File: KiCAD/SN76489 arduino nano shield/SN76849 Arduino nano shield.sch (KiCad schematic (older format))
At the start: 10 parts, among them J1 Arduino_sn, P1 Audio_uit, P3 I2C, U1 PCF8574, U2 LM358, U3 SN76489

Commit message: Printplaat 20180601 0.5 laat maak
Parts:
- added J2: audio_debug, Socket_Strips:Socket_Strip_Straight_1x02_Pitch2.54mm, symbol Conn_01x02
- C2, C3: footprint Capacitors_SMD:C_1210 -> Capacitors_THT:CP_Radial_D8.0mm_P2.50mm
- R2: footprint Resistors_SMD:R_1206 -> w_pth_resistors:RC03
- RV1: footprint w_pth_resistors:trimmer_alps-rk09k1130ah1 -> w_pth_resistors:trimmer_ecp_ca9-v10
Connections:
- net GND: now also J2.2 (Pin_2)
- net at C2.2, R2.2: now also J2.1 (Pin_1)
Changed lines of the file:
@@
 Sheet 1 1
 Title "SN76489 geluid shield vir Arduino Nano"
-Date "2018-04-05"
-Rev "0.3 20180405"
+Date "2018-05-16"
+Rev "20180601 0.5"
 Comp "EasyLab4Kids"
 Comment1 "Ontwerp: Michiel Erasmus"
@@
 F 0 "C3" H 7110 4460 38  0000 L CNN
 F 1 "CP_220uF" V 6990 4240 30  0000 L CNN
-F 2 "Capacitors_SMD:C_1210" H 7100 4390 50  0001 C CNN
+F 2 "Capacitors_THT:CP_Radial_D8.0mm_P2.50mm" H 7100 4390 50  0001 C CNN
 F 3 "" H 7100 4390 50  0001 C CNN
 	1    7100 4390
@@
 F 0 "RV1" H 7490 4310 38  0000 C CNN
 F 1 "POT_50k" H 7490 4390 30  0000 C CNN
-F 2 "w_pth_resistors:trimmer_alps-rk09k1130ah1" H 7490 4390 50  0001 C CNN
+F 2 "w_pth_resistors:trimmer_ecp_ca9-v10" H 7490 4390 50  0001 C CNN
 F 3 "" H 7490 4390 50  0000 C CNN
 	1    7490 4390
@@
 F 0 "R2" H 6090 4620 38  0000 L CNN
 F 1 "R1k" V 6060 4560 30  0000 L CNN
-F 2 "Resistors_SMD:R_1206" H 6060 4600 50  0001 C CNN
+F 2 "w_pth_resistors:RC03" H 6060 4600 50  0001 C CNN
 F 3 "" H 6060 4600 50  0000 C CNN
 	1    6060 4600
@@
 F 0 "C2" H 6070 4990 38  0000 L CNN
 F 1 "CP_10uF" V 5950 4770 30  0000 L CNN
-F 2 "Capacitors_SMD:C_1210" H 6060 4920 50  0001 C CNN
+F 2 "Capacitors_THT:CP_Radial_D8.0mm_P2.50mm" H 6060 4920 50  0001 C CNN
 F 3 "" H 6060 4920 50  0001 C CNN
 	1    6060 4920
@@
 	1    0    0    -1
 $EndComp
+$Comp
+L Conn_01x02 J2
+U 1 1 5AEF7BF4
+P 5140 4730
+F 0 "J2" H 5140 4830 50  0000 C CNN
+F 1 "audio_debug" H 5140 4530 30  0000 C CNN
+F 2 "Socket_Strips:Socket_Strip_Straight_1x02_Pitch2.54mm" H 5140 4730 50  0001 C CNN
+F 3 "" H 5140 4730 50  0001 C CNN
+	1    5140 4730
+	-1   0    0    1
+$EndComp
 Wire Wire Line
 	5600 1110 6050 1110
@@
 	5650 1610 5650 1810
 Connection ~ 5650 1810
+Wire Wire Line
+	5340 4730 6060 4730
+Connection ~ 6060 4730
+Wire Wire Line
+	5340 4630 5950 4630
+Connection ~ 5950 4630
 $EndSCHEMATC

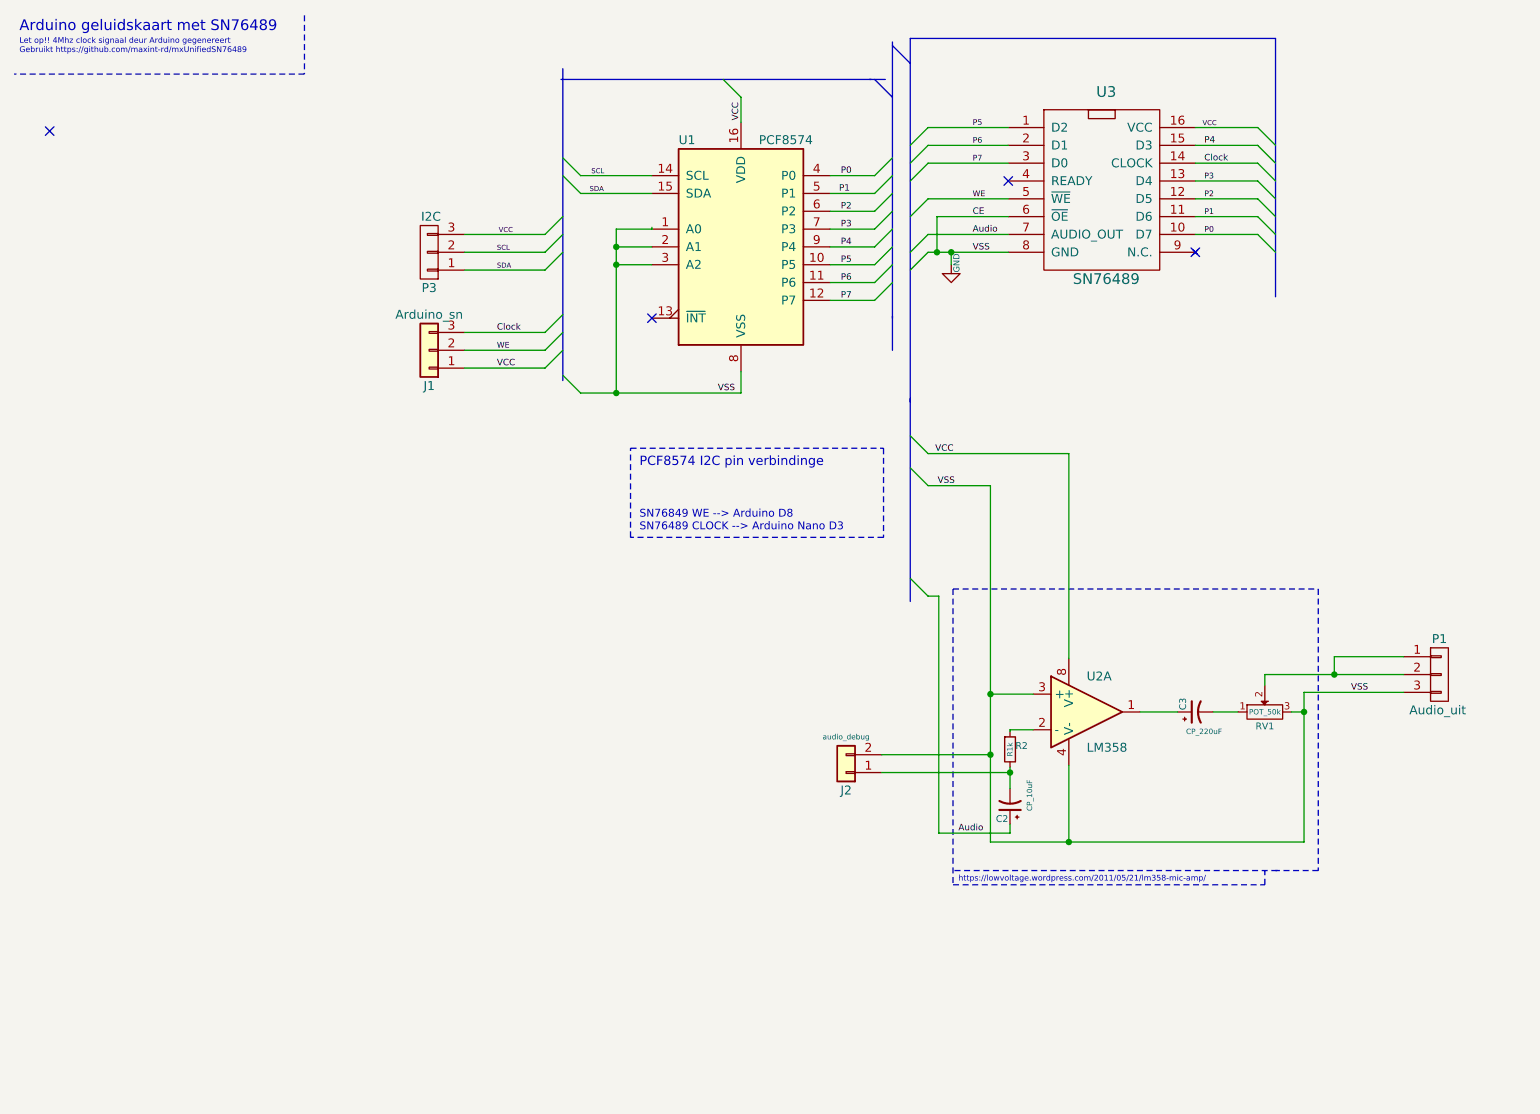
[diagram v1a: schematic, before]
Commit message: toevoeging OpAmp schema en PCB 20180617 0.7
daar is nog een bug. Op printplaat capacitor C1 posetief niet
verobonden!
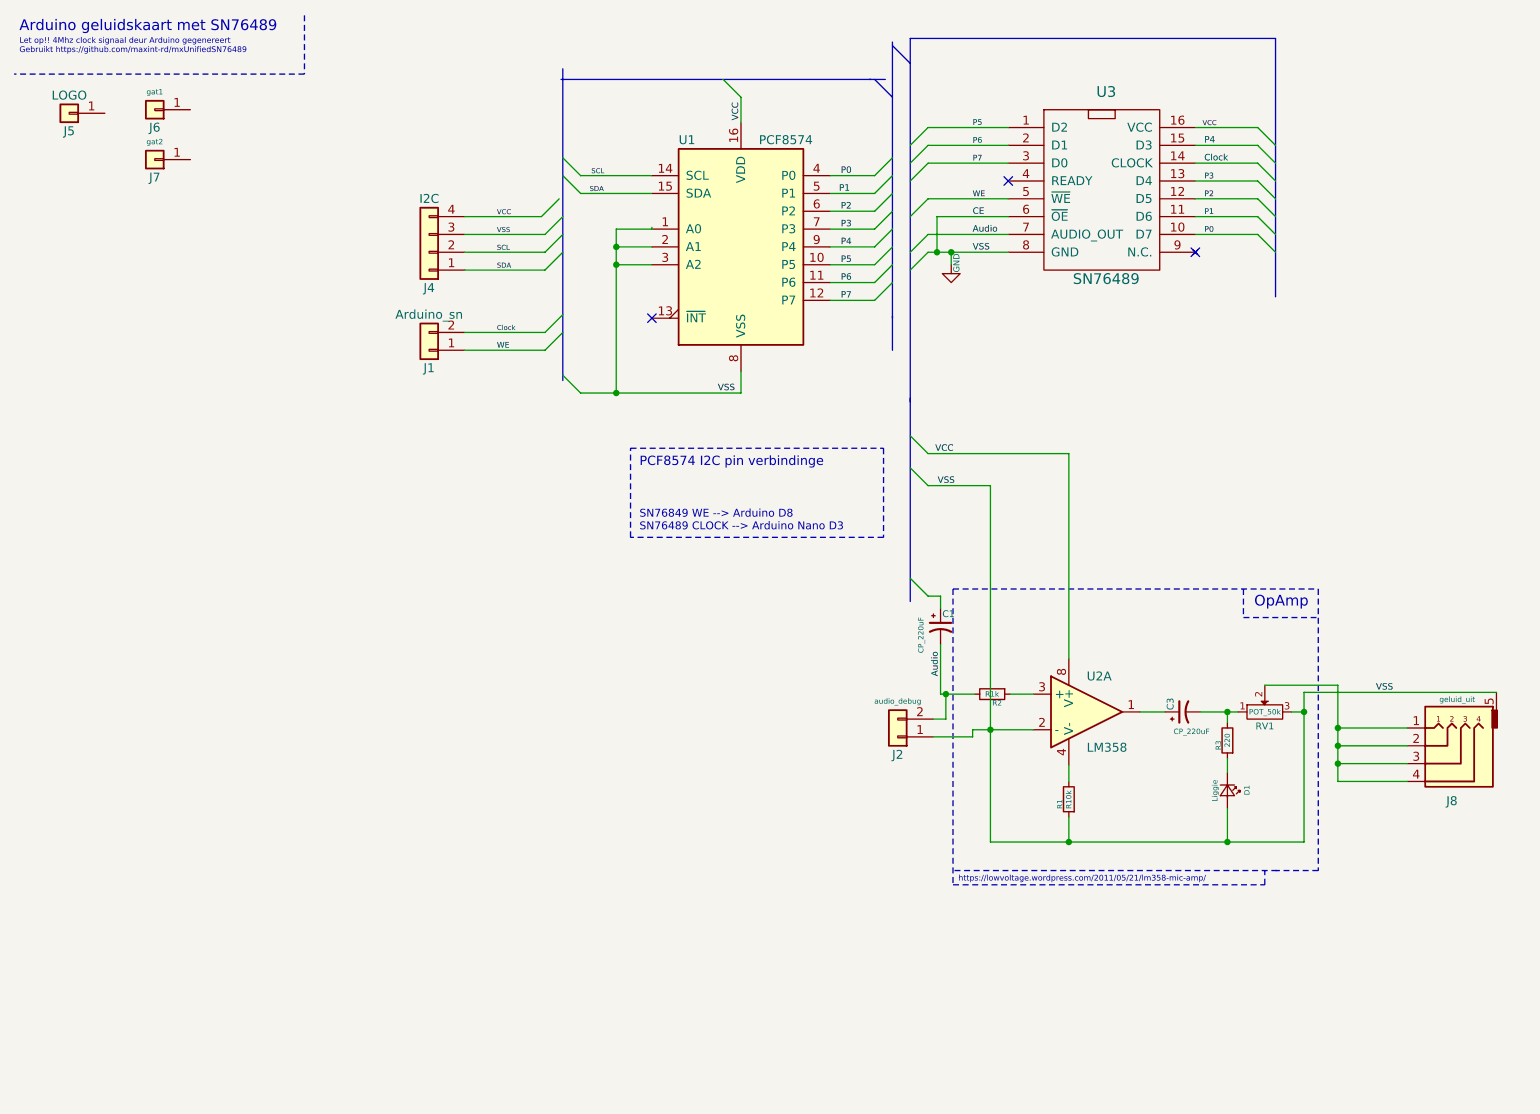
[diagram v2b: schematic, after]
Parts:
- removed C2: CP_10uF, Capacitors_THT:CP_Radial_D8.0mm_P2.50mm, symbol CP1_Small
- removed J1: Arduino_sn, Socket_Strips:Socket_Strip_Angled_1x03_Pitch2.54mm, symbol Conn_01x03
- removed P1: Audio_uit, Socket_Strips:Socket_Strip_Angled_1x03_Pitch2.54mm, symbol CONN_01X03
- removed P3: I2C, Socket_Strips:Socket_Strip_Angled_1x03_Pitch2.54mm, symbol CONN_01X03
- added C1: CP_220uF, Capacitors_THT:CP_Radial_D8.0mm_P2.50mm, symbol CP1_Small
- added D1: Liggie, LEDs:LED_D3.0mm, symbol LED_Small
- added J1: Arduino_sn, Pin_Headers:Pin_Header_Angled_1x02_Pitch2.54mm, symbol Conn_01x02
- added J4: I2C, Pin_Headers:Pin_Header_Angled_1x04_Pitch2.54mm, symbol Conn_01x04
- added J5: LOGO, lib_michiel:Sovjet_simpits_logo01, symbol Conn_01x01
- added J6: gat1, Mounting_Holes:MountingHole_2.5mm_Pad, symbol Conn_01x01
- added J7: gat2, Mounting_Holes:MountingHole_2.5mm_Pad, symbol Conn_01x01
- added J8: geluid_uit, lib_michiel:3.5mm_stereo_TRS_jack_A-853_Tayda_, symbol Audio-Jack-5
- added R1: R10k, w_pth_resistors:RC03, symbol R_Small
- added R3: 220, w_pth_resistors:RC03, symbol R_Small
- J2: footprint Socket_Strips:Socket_Strip_Straight_1x02_Pitch2.54mm -> Pin_Headers:Pin_Header_Angled_1x02_Pitch2.54mm
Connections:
- net Audio: now also J2.2 (Pin_2), R2.2, C1.2
- net Clock: now also J1.2 (Pin_2)
- net GND: now also J2.1 (Pin_1), U2.2 (-), D1.2 (A), J4.3 (Pin_3), J8.5, R1.1; no longer J2.2 (Pin_2), U2.3 (+), U2.4 (V-)
- net SCL: now also J4.2 (Pin_2)
- net SDA: now also J4.1 (Pin_1)
- net VCC: now also J4.4 (Pin_4)
- net WE: now also J1.1 (Pin_1)
- net at RV1.2: now also J8.1, J8.2, J8.3, J8.4
- net at C3.2, RV1.1: now also R3.2
- net at R2.1: now also U2.3 (+); no longer U2.2 (-)
- new net: R1.2, U2.4 (V-)
- new net: D1.1 (K), R3.1
- no-connect marks 4 -> 3
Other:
- note added: "OpAmp"
- moved on the sheet: C3, J2, R2

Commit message: DERC fails opgelost 20180617 0.7.01
'n paar nets ontbreekte conneksies op de printplaat.
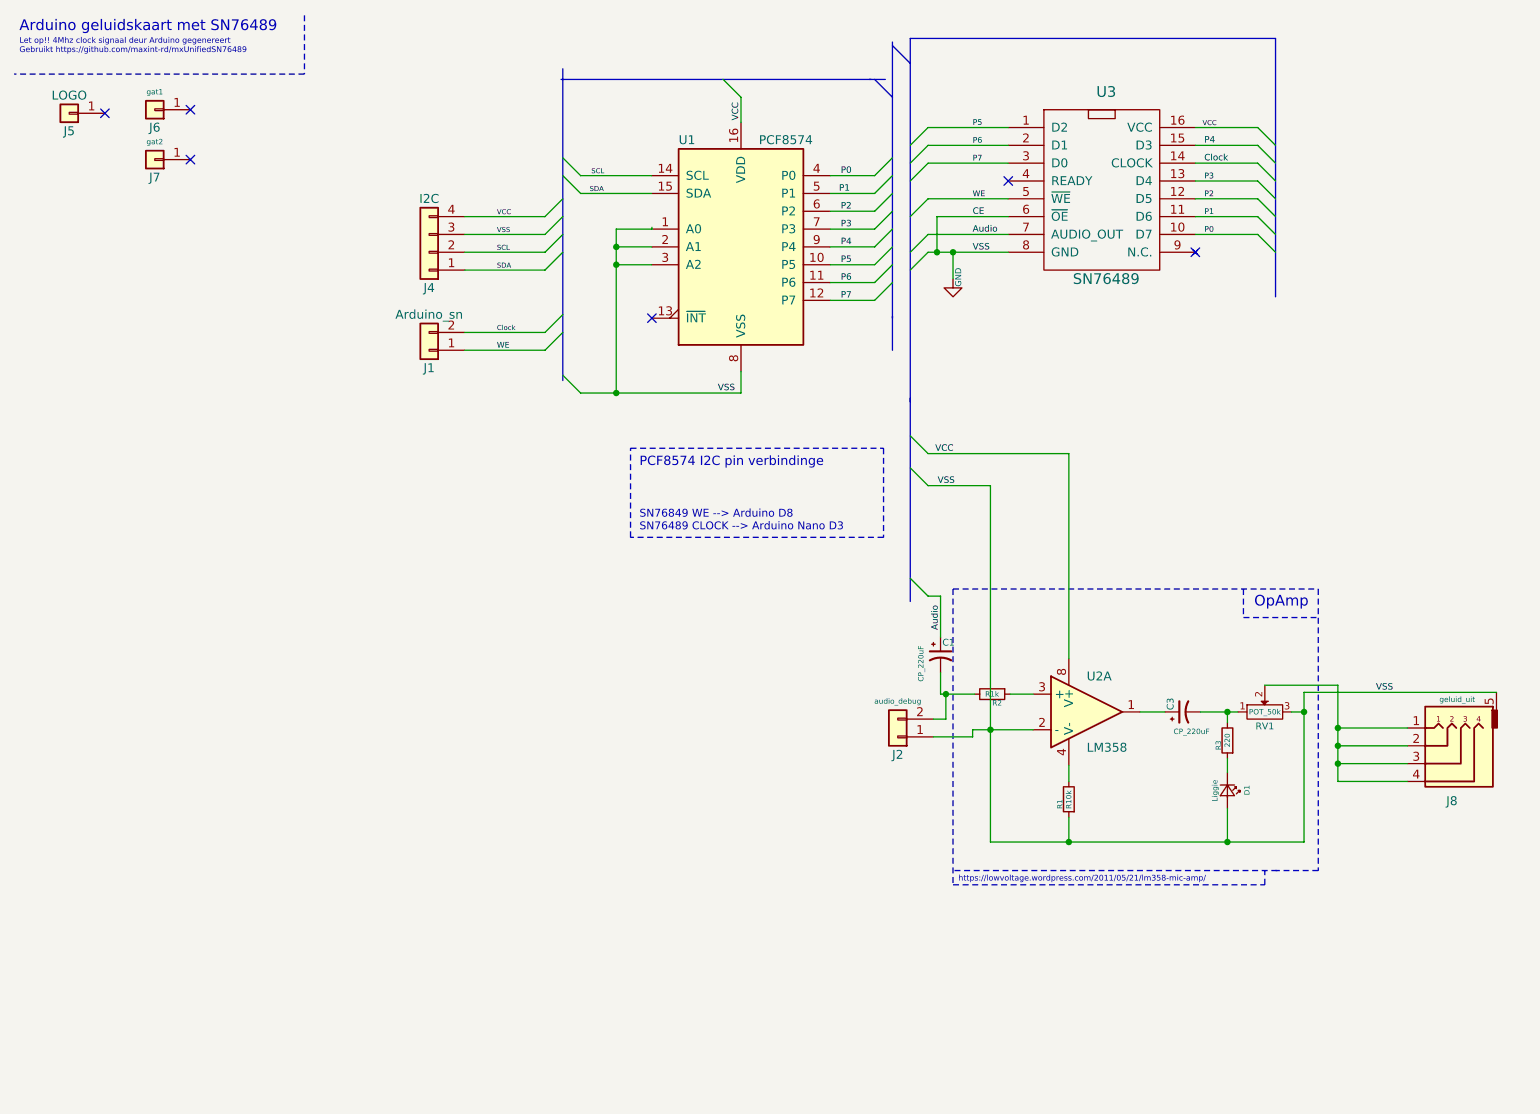
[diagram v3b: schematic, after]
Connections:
- net Audio: now also C1.1; no longer C1.2, J2.2 (Pin_2), R2.2
- new net: C1.2, J2.2 (Pin_2), R2.2
- no-connect marks 3 -> 6
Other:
- moved on the sheet: C1
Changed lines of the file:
@@
 Sheet 1 1
 Title "SN76489 geluid shield vir Arduino Nano"
-Date "2018-06-17"
-Rev "20180617 0.7"
+Date "2018-06-24"
+Rev "20180617 0.7.01"
 Comp "EasyLab4Kids"
 Comment1 "Ontwerp: Michiel Erasmus"
@@
 Text Label 5750 3120 2    36   ~ 0
 VSS
-Entry Wire Line
-	5500 3020 5600 3120
 Text Label 5640 2940 0    36   ~ 0
 VCC
@@
 Text Notes 5770 5350 0    32   ~ 0
 https://lowvoltage.wordpress.com/2011/05/21/lm358-mic-amp/
-Entry Wire Line
-	5500 3640 5600 3740
-Text Label 5670 4190 1    36   ~ 0
+Text Label 5670 3930 1    36   ~ 0
 Audio
 $Comp
 L GND #PWR01
 U 1 1 5A9BDD7A
-P 5730 1880
-F 0 "#PWR01" H 5730 1630 50  0001 C CNN
-F 1 "GND" V 5760 1890 34  0000 C CNN
-F 2 "" H 5730 1880 50  0000 C CNN
-F 3 "" H 5730 1880 50  0000 C CNN
-	1    5730 1880
+P 5740 1960
+F 0 "#PWR01" H 5740 1710 28  0001 C CNN
+F 1 "GND" V 5770 1970 34  0000 C CNN
+F 2 "" H 5740 1960 50  0000 C CNN
+F 3 "" H 5740 1960 50  0000 C CNN
+	1    5740 1960
 	1    0    0    -1
 $EndComp
@@
 $EndComp
 Entry Wire Line
-	3430 1610 3530 1510
+	3450 1610 3550 1510
 Text Label 3180 1710 0    28   ~ 0
 VSS
@@
 	-1   0    0    1
 $EndComp
+$Comp
+L CP1_Small C1
+U 1 1 5B26BD41
+P 5670 4070
+F 0 "C1" H 5680 4140 38  0000 L CNN
+F 1 "CP_220uF" V 5560 3920 30  0000 L CNN
+F 2 "Capacitors_THT:CP_Radial_D8.0mm_P2.50mm" H 5670 4070 50  0001 C CNN
+F 3 "" H 5670 4070 50  0001 C CNN
+	1    5670 4070
+	1    0    0    -1
+$EndComp
+Entry Wire Line
+	5500 3640 5600 3740
+Entry Wire Line
+	5500 3020 5600 3120
+NoConn ~ 1460 1010
+NoConn ~ 1460 1290
 Wire Wire Line
 	5600 1110 6050 1110
@@
 	5600 1310 6050 1310
 Wire Wire Line
-	5600 1510 6050 1510
-Wire Wire Line
-	5600 1810 6050 1810
-Wire Wire Line
 	7100 1210 7450 1210
 Wire Wire Line
@@
 	7100 1710 7450 1710
 Wire Bus Line
-	5500 610  5500 2650
-Wire Bus Line
 	7550 610  7550 2060
 Wire Bus Line
@@
 	3000 2260 3450 2260
 Wire Wire Line
-	3000 2360 3450 2360
-Wire Wire Line
 	3450 1710 3000 1710
 Wire Wire Line
@@
 Wire Notes Line
 	2100 810  470  810
-Wire Wire Line
-	7100 1110 7450 1110
 Wire Wire Line
 	5050 1580 5300 1580
@@
 	3850 1680 3850 2600
 Connection ~ 3850 2600
-Wire Bus Line
-	5500 2630 5500 3770
 Wire Notes Line
 	7560 5280 5740 5280
@@
 Wire Notes Line
 	7490 5360 7490 5280
+Connection ~ 5950 4490
+Wire Wire Line
+	6190 4290 6060 4290
+Wire Wire Line
+	6390 4980 6390 5120
+Connection ~ 6390 5120
+Wire Wire Line
+	5670 4290 5860 4290
+Wire Wire Line
+	5630 4430 5700 4430
+Wire Wire Line
+	5700 4430 5700 4290
+Connection ~ 5700 4290
+Wire Wire Line
+	5630 4530 5850 4530
+Wire Wire Line
+	5850 4530 5850 4490
+Wire Notes Line
+	7370 3700 7370 3860
+Wire Notes Line
+	7370 3860 7780 3860
+Wire Wire Line
+	6930 4390 6790 4390
+Wire Wire Line
+	7130 4390 7340 4390
+Wire Wire Line
+	7280 4450 7280 4390
+Connection ~ 7280 4390
+Wire Wire Line
+	7280 4650 7280 4730
+Wire Wire Line
+	7280 4930 7280 5120
+Connection ~ 7280 5120
+Wire Wire Line
+	7490 4240 7900 4240
+Wire Wire Line
+	7900 4240 7900 4780
+Wire Wire Line
+	7900 4480 8290 4480
+Wire Wire Line
+	7900 4580 8290 4580
+Connection ~ 7900 4480
+Wire Wire Line
+	7900 4680 8290 4680
+Connection ~ 7900 4580
+Wire Wire Line
+	7900 4780 8290 4780
+Connection ~ 7900 4680
+Wire Wire Line
+	5670 3740 5670 3970
+Wire Bus Line
+	5500 610  5500 2650
 Wire Wire Line
 	5600 3740 5670 3740
-Wire Wire Line
-	5730 1880 5730 1810
-Connection ~ 5730 1810
+Wire Bus Line
+	5500 2630 5500 3770
+Wire Wire Line
+	5670 4290 5670 4170
+Wire Wire Line
+	7100 1110 7450 1110
+Wire Wire Line
+	5600 1810 6050 1810
 Wire Wire Line
 	5650 1610 5650 1810
 Connection ~ 5650 1810
-Connection ~ 5950 4490
-Wire Wire Line
-	6190 4290 6060 4290
-Wire Wire Line
-	6390 4980 6390 5120
-Connection ~ 6390 5120
+Wire Wire Line
+	5740 1960 5740 1810
+Connection ~ 5740 1810
+Wire Wire Line
+	3000 2360 3450 2360
+Wire Wire Line
+	5600 1510 6050 1510
+Wire Wire Line
+	3000 1610 3450 1610
+NoConn ~ 980  1030
 Wire Wire Line
 	6390 4690 6390 4780
-Wire Wire Line
-	5670 4010 5670 4290
-Wire Wire Line
-	5670 4290 5860 4290
-Wire Wire Line
-	5630 4430 5700 4430
-Wire Wire Line
-	5700 4430 5700 4290
-Connection ~ 5700 4290
-Wire Wire Line
-	5630 4530 5850 4530
-Wire Wire Line
-	5850 4530 5850 4490
-Wire Wire Line
-	3000 1610 3430 1610
-Wire Notes Line
-	7370 3700 7370 3860
-Wire Notes Line
-	7370 3860 7780 3860
-Wire Wire Line
-	6930 4390 6790 4390
-Wire Wire Line
-	7130 4390 7340 4390
-Wire Wire Line
-	7280 4450 7280 4390
-Connection ~ 7280 4390
-Wire Wire Line
-	7280 4650 7280 4730
-Wire Wire Line
-	7280 4930 7280 5120
-Connection ~ 7280 5120
-Wire Wire Line
-	7490 4240 7900 4240
-Wire Wire Line
-	7900 4240 7900 4780
-Wire Wire Line
-	7900 4480 8290 4480
-Wire Wire Line
-	7900 4580 8290 4580
-Connection ~ 7900 4480
-Wire Wire Line
-	7900 4680 8290 4680
-Connection ~ 7900 4580
-Wire Wire Line
-	7900 4780 8290 4780
-Connection ~ 7900 4680
-Wire Wire Line
-	5670 3740 5670 3810
-$Comp
-L CP1_Small C1
-U 1 1 5B26BD41
-P 5670 3910
-F 0 "C1" H 5680 3980 38  0000 L CNN
-F 1 "CP_220uF" V 5560 3760 30  0000 L CNN
-F 2 "Capacitors_THT:CP_Radial_D8.0mm_P2.50mm" H 5670 3910 50  0001 C CNN
-F 3 "" H 5670 3910 50  0001 C CNN
-	1    5670 3910
-	1    0    0    -1
-$EndComp
 $EndSCHEMATC

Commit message: EasySynth SN87489 synth 0.7.01 printplaatversie
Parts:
- added J?: OLED_128x32, Pin_Headers:Pin_Header_Angled_1x04_Pitch2.54mm, symbol Conn_01x04
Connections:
- net GND: now also J8.1, J?.2 (Pin_2); no longer J8.5
- net SCL: now also J?.3 (Pin_3)
- net SDA: now also J?.4 (Pin_4)
- net VCC: now also J?.1 (Pin_1)
- net at J8.2, J8.3, J8.4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: now also J8.5; no longer J8.1
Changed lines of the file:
@@
 LIBS:arduino
 LIBS:easylab4kids
+LIBS:trs_jack
 LIBS:SN76849 Arduino nano shield-cache
 EELAYER 25 0
@@
 Sheet 1 1
 Title "SN76489 geluid shield vir Arduino Nano"
-Date "2018-06-24"
-Rev "20180617 0.7.01"
+Date "2018-07-09"
+Rev "20180617 0.7.02"
 Comp "EasyLab4Kids"
 Comment1 "Ontwerp: Michiel Erasmus"
@@
 Entry Wire Line
 	5300 1680 5400 1580
-Text Label 8210 4280 2    36   ~ 0
+Text Label 8210 4480 2    36   ~ 0
 VSS
 Text Label 5110 1980 0    36   ~ 0
@@
 	5050 1680 5300 1680
 Wire Wire Line
-	7710 4280 8790 4280
-Wire Wire Line
 	5050 1980 5300 1980
 Wire Notes Line
@@
 	5950 3120 5950 5120
 Wire Wire Line
-	7710 5120 7710 4280
-Wire Wire Line
 	5600 2940 6390 2940
 Wire Wire Line
@@
 Wire Wire Line
 	7640 4390 7710 4390
-Connection ~ 7710 4390
 Wire Notes Line
 	5740 3700 7790 3700
@@
 	7490 4240 7900 4240
 Wire Wire Line
-	7900 4240 7900 4780
-Wire Wire Line
-	7900 4480 8290 4480
+	7900 4240 7900 4950
 Wire Wire Line
 	7900 4580 8290 4580
-Connection ~ 7900 4480
 Wire Wire Line
 	7900 4680 8290 4680
@@
 Wire Wire Line
 	6390 4690 6390 4780
+Wire Wire Line
+	8790 4280 8790 4200
+Wire Wire Line
+	8790 4200 8860 4200
+Wire Wire Line
+	8860 4200 8860 4950
+Wire Wire Line
+	8860 4950 7900 4950
+Connection ~ 7900 4780
+Wire Wire Line
+	7710 4390 7710 5120
+Wire Wire Line
+	7710 4480 8290 4480
+Connection ~ 7710 4480
+$Comp
+L Conn_01x04 J?
+U 1 1 5B43DC64
+P 6120 2390
+F 0 "J?" H 6120 2590 50  0000 C CNN
+F 1 "OLED_128x32" H 6120 2090 38  0000 C CNN
+F 2 "Pin_Headers:Pin_Header_Angled_1x04_Pitch2.54mm" H 6120 2390 50  0001 C CNN
+F 3 "" H 6120 2390 50  0001 C CNN
+	1    6120 2390
+	1    0    0    -1
+$EndComp
+Entry Wire Line
+	5500 2190 5600 2290
+Entry Wire Line
+	5500 2290 5600 2390
+Entry Wire Line
+	5500 2390 5600 2490
+Entry Wire Line
+	5500 2490 5600 2590
+Wire Wire Line
+	5600 2290 5920 2290
+Wire Wire Line
+	5920 2390 5600 2390
+Wire Wire Line
+	5600 2490 5920 2490
+Wire Wire Line
+	5920 2590 5600 2590
+Text Label 5760 2290 0    28   ~ 0
+VCC
+Text Label 5760 2390 0    28   ~ 0
+VSS
+Text Label 5760 2490 0    28   ~ 0
+SCL
+Text Label 5760 2590 0    28   ~ 0
+SDA
 $EndSCHEMATC
